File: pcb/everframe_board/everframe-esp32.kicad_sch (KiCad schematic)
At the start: 1 part, among them U1 MODULE-SEEEDUINO-XIAO-ESP32S3

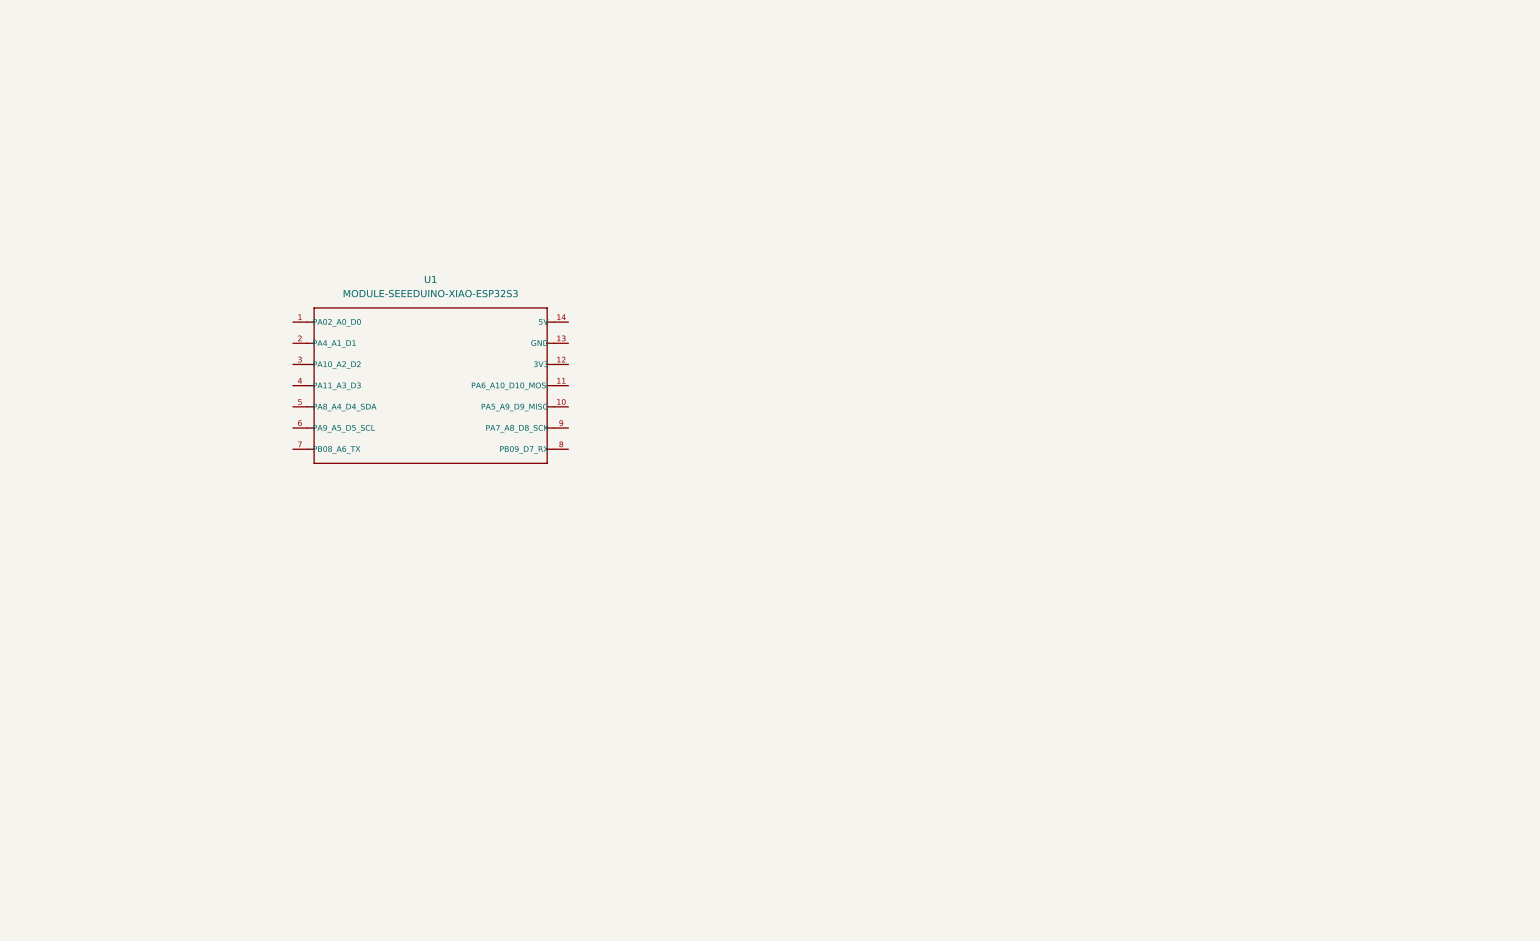
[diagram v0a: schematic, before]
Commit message: Finished sch, started layout 2L only
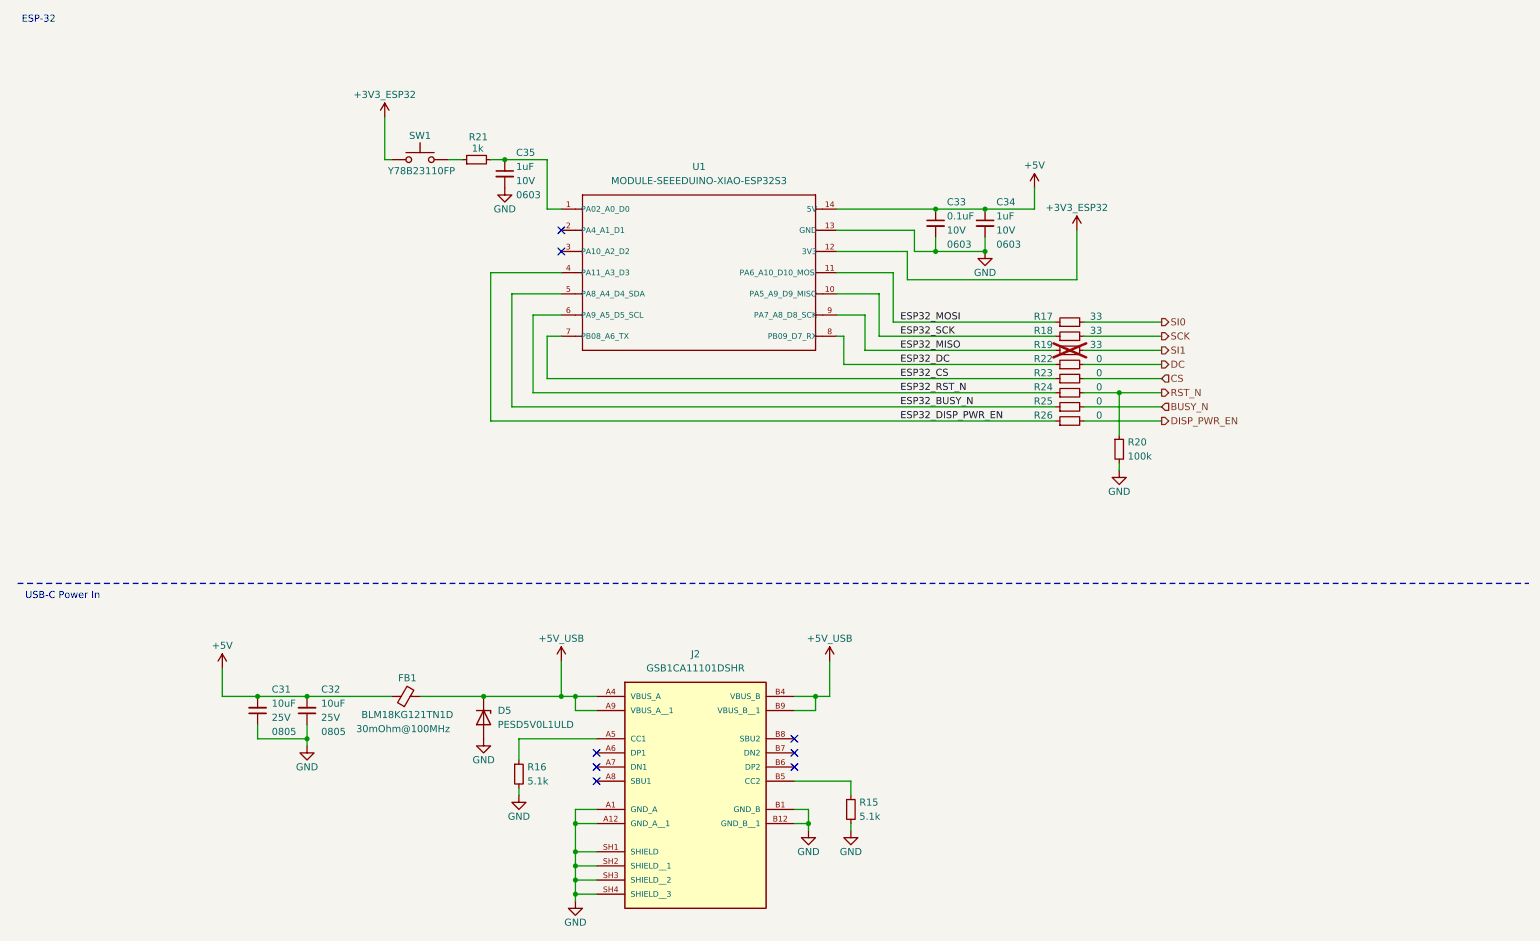
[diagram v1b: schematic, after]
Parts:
- added C31, C32: 10uF, Capacitor_SMD:C_0805_2012Metric, symbol Device:C_Small
- added C33: 0.1uF, Capacitor_SMD:C_0603_1608Metric, symbol Device:C_Small
- added C34, C35: 1uF, Capacitor_SMD:C_0603_1608Metric, symbol Device:C_Small
- added D5: PESD5V0L1ULD, Diode_SMD:D_SOD-882D, symbol Diode:PESD5V0L1ULD
- added FB1: 30mOhm@100MHz, Inductor_SMD:L_0603_1608Metric, symbol Device:FerriteBead_Small
- added J2: GSB1CA11101DSHR, everframe_library.footprints:AMPHENOL_GSB1CA11101DSHR, symbol everframe_library:GSB1CA11101DSHR
- added R15, R16: 5.1k, Resistor_SMD:R_0603_1608Metric, symbol Device:R_Small
- added R17, R18, R19: 33, Resistor_SMD:R_0603_1608Metric, symbol Device:R_Small
- added R20: 100k, Resistor_SMD:R_0603_1608Metric, symbol Device:R_Small
- added R21: 1k, Resistor_SMD:R_0603_1608Metric, symbol Device:R_Small
- added R22, R23, R24, R25, R26: 0, Resistor_SMD:R_0603_1608Metric, symbol Device:R_Small
- added SW1: SW_Push, Button_Switch_SMD:SW_Push_1P1T_NO_CK_KMR2, symbol Switch:SW_Push
- U1: footprint MOUDLE14P-SMD-2.54-21X17.8MM -> everframe_library.footprints:MOUDLE14P-SMD-2.54-21X17.8MM
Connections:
- net at U1.1 (PA02_A0_D0): now also C35.1, R21.2
- net ESP32_SCK: now reaches U1.10 (PA5_A9_D9_MISO)
- net ESP32_SCK: now also R18.1
- net ESP32_MOSI: now reaches U1.11 (PA6_A10_D10_MOSI)
- net ESP32_MOSI: now also R17.1
- net +3V3_ESP32: now reaches U1.12 (3V3)
- net +3V3_ESP32: now also SW1.1
- net GND: now reaches U1.13 (GND)
- net GND: now also C31.1, C32.1, C33.2, C34.2, C35.2, D5.2 (A), J2.A1 (GND_A), J2.A12 (GND_A__1), J2.B1 (GND_B), J2.B12 (GND_B__1), J2.SH1 (SHIELD), J2.SH2 (SHIELD__1), J2.SH3 (SHIELD__2), J2.SH4 (SHIELD__3), R15.2, R16.2, R20.2
- net +5V: now reaches U1.14 (5V)
- net +5V: now also C31.2, C32.2, C33.1, C34.1, FB1.1
- net ESP32_DISP_PWR_EN: now reaches U1.4 (PA11_A3_D3)
- net ESP32_DISP_PWR_EN: now also R26.1
- net ESP32_BUSY_N: now reaches U1.5 (PA8_A4_D4_SDA)
- net ESP32_BUSY_N: now also R25.1
- net ESP32_RST_N: now reaches U1.6 (PA9_A5_D5_SCL)
- net ESP32_RST_N: now also R24.1
- net ESP32_CS: now reaches U1.7 (PB08_A6_TX)
- net ESP32_CS: now also R23.1
- net ESP32_DC: now reaches U1.8 (PB09_D7_RX)
- net ESP32_DC: now also R22.1
- net ESP32_MISO: now reaches U1.9 (PA7_A8_D8_SCK)
- net ESP32_MISO: now also R19.1
- new net: J2.A5 (CC1), R16.1
- new net: R21.1, SW1.2
- new net: J2.B5 (CC2), R15.1
- new net +5V_USB: D5.1 (K), FB1.2, J2.A4 (VBUS_A), J2.A9 (VBUS_A__1), J2.B4 (VBUS_B), J2.B9 (VBUS_B__1)
- new net BUSY_N: R25.2
- new net CS: R23.2
- new net DC: R22.2
- new net DISP_PWR_EN: R26.2
- new net RST_N: R20.1, R24.2
- new net SCK: R18.2
- new net SI0: R17.2
- new net SI1: R19.2
- no-connect marks 0 -> 8
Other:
- note added: "ESP-32"
- note added: "USB-C Power In"
- moved on the sheet: U1

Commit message: Routed board, mostly need checks
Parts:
- removed U1: MODULE-SEEEDUINO-XIAO-ESP32S3, everframe_library.footprints:MOUDLE14P-SMD-2.54-21X17.8MM, symbol everframe_library:MODULE-SEEEDUINO-XIAO-ESP32S3
- added J3: SM02B-GHS-TB, Connector_JST:JST_GH_SM02B-GHS-TB_1x02-1MP_P1.25mm_Horizontal, symbol Connector:Conn_01x02_Pin
- added U1: XIAO-ESP32-S3-SMD, seed_studio:XIAO-ESP32S3-SMD, symbol xiao_seed:XIAO-ESP32-S3-SMD
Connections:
- net +3V3_ESP32: now also U1.12 (3V3)
- net +5V: now also U1.14 (5V)
- net ESP32_BUSY_N: now also U1.5 (GPIO5_A4_D4_SDA)
- net ESP32_CS: now also U1.7 (GPIO43_A6_D6_TX)
- net ESP32_DC: now also U1.8 (GPIO44_D7_RX)
- net ESP32_DISP_PWR_EN: now also U1.4 (GPIO4_A3_D3)
- net ESP32_MISO: now also U1.9 (GPIO7_A8_D8_SCK)
- net ESP32_MOSI: now also U1.11 (GPIO9_A10_D10_MOSI)
- net ESP32_RST_N: now also U1.6 (GPIO6_A5_D5_SCL)
- net ESP32_SCK: now also U1.10 (GPIO8_A9_D9_MISO)
- net GND: now also J3.1 (Pin_1), U1.13 (GND), U1.16 (GND)
- net at C35.1, R21.2: now also U1.1 (GPIO1_A0_D0)
- new net VBAT: J3.2 (Pin_2), U1.15 (BAT)
- no-connect marks 8 -> 15
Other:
- moved on the sheet: C33, C34, C35, R17, R18, R19, R20, R21, R22, R23, R24, R25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

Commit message: Update pcb and create packaging design
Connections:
- no-connect marks 15 -> 17
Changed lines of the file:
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@@
+	)
+	(no_connect
+		(at 116.84 41.91)
 	)
 	(no_connect
@@
 	)
 	(no_connect
+		(at 116.84 45.72)
+	)
+	(no_connect

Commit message: Some unused google cloud function code added, esp32 idf embedded project added with display drivers, pcb fab exported
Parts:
- R18: now not fitted
- R19: now fitted
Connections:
- net ESP32_MISO: now also R18.1, U1.10 (GPIO8_A9_D9_MISO); no longer R19.1, U1.9 (GPIO7_A8_D8_SCK)
- net ESP32_SCK: now also R19.1, U1.9 (GPIO7_A8_D8_SCK); no longer R18.1, U1.10 (GPIO8_A9_D9_MISO)
- net SCK: now also R19.2; no longer R18.2
- net SI1: now also R18.2; no longer R19.2
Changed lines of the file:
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@@
 	(title_block
 		(title "Everframe Mainboard")
-		(rev "0.0.1")
+		(date "2025-11-24")
+		(rev "1.0.0")
 	)
 	(text "USB-C Power In"
@@
 		)
 	)
-	(label "ESP32_MISO"
+	(label "ESP32_SCK"
 		(at 180.34 63.5 0)
 		(effects
@@
 		)
 	)
-	(label "ESP32_SCK"
+	(label "ESP32_MISO"
 		(at 180.34 60.96 0)
 		(effects
@@
 		)
 	)
-	(hierarchical_label "SCK"
+	(hierarchical_label "SI1"
 		(shape output)
 		(at 227.33 60.96 0)
@@
 		)
 	)
-	(hierarchical_label "SI1"
+	(hierarchical_label "SCK"
 		(shape output)
 		(at 227.33 63.5 0)
@@
 		(in_bom yes)
 		(on_board yes)
-		(dnp no)
+		(dnp yes)
 		(property "Reference" "R18"
 			(at 207.772 59.944 90)
@@
 		(in_bom yes)
 		(on_board yes)
-		(dnp yes)
+		(dnp no)
 		(property "Reference" "R19"
 			(at 207.772 62.484 90)
